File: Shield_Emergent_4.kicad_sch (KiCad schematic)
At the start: 32 parts, among them J1 TF31-18S-0.5SH_800_, J2 Conn_01x04_Socket, J3 TF31-18S-0.5SH_800_, J5 Conn_01x02_Socket, J6 Conn_01x02_Socket, U3 SP3012-06UTG, U4 SP3012-06UTG, X1 USB_C_24pins

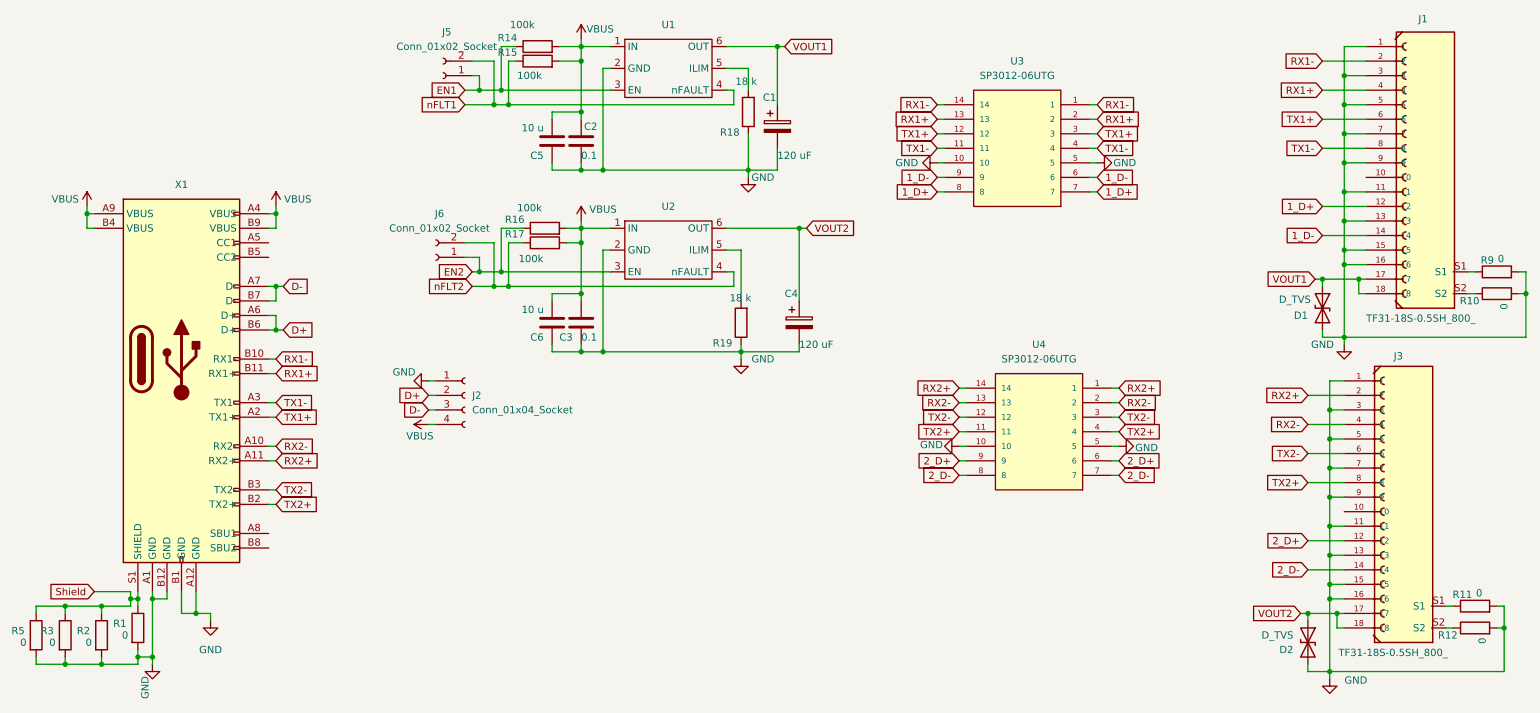
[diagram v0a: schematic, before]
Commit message: v0.2 draft routing
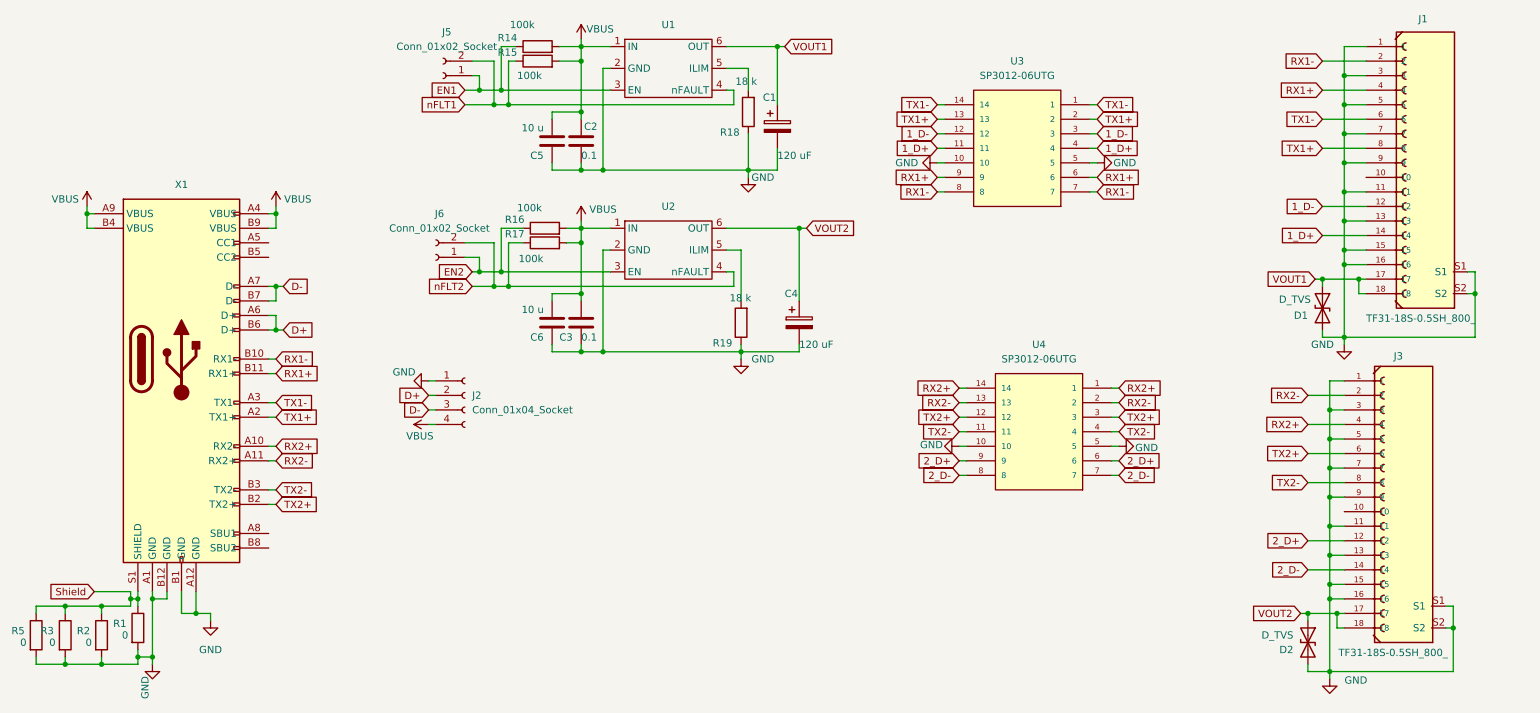
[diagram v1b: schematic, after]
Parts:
- removed R10, R11, R12, R9: 0, Resistor_SMD:R_0201_0603Metric_Pad0.64x0.40mm_HandSolder, symbol Device:R
- C2, C3, C5, C6: footprint Capacitor_SMD:C_0603_1608Metric_Pad1.08x0.95mm_HandSolder -> Capacitor_SMD:C_0402_1005Metric
- R14, R15, R16, R17, R18, R19: footprint Resistor_SMD:R_0603_1608Metric_Pad0.98x0.95mm_HandSolder -> Resistor_SMD:R_0402_1005Metric
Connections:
- net 1_D+: now also J1.14, U3.11, U3.4; no longer J1.12, U3.7, U3.8
- net 1_D-: now also J1.12, U3.12, U3.3; no longer J1.14, U3.6, U3.9
- net GND: now also J1.S1, J1.S2, J3.S1, J3.S2
- net RX1+: now also U3.6, U3.9; no longer U3.13, U3.2
- net RX1-: now also U3.7, U3.8; no longer U3.1, U3.14
- net RX2+: now also J3.4, X1.A10 (RX2-); no longer J3.2, X1.A11 (RX2+)
- net RX2-: now also J3.2, X1.A11 (RX2+); no longer J3.4, X1.A10 (RX2-)
- net TX1+: now also J1.8, U3.13, U3.2; no longer J1.6, U3.12, U3.3
- net TX1-: now also J1.6, U3.1, U3.14; no longer J1.8, U3.11, U3.4
- net TX2+: now also J3.6, U4.12, U4.3; no longer J3.8, U4.11, U4.4
- net TX2-: now also J3.8, U4.11, U4.4; no longer J3.6, U4.12, U4.3

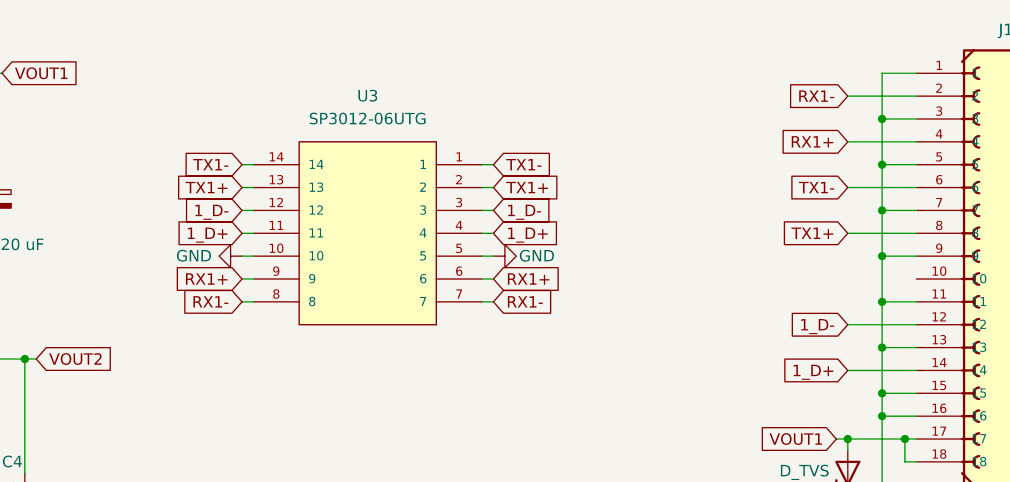
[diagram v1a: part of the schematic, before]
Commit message: v0.3 conceptual routing was added
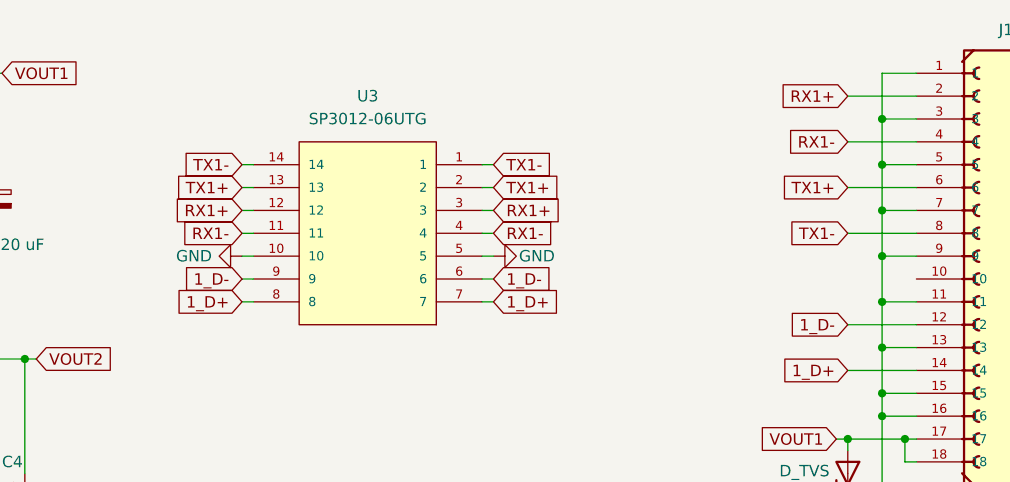
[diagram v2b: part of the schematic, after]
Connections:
- net 1_D+: now also U3.7, U3.8; no longer U3.11, U3.4
- net 1_D-: now also U3.6, U3.9; no longer U3.12, U3.3
- net RX1+: now also J1.2, U3.12, U3.3; no longer J1.4, U3.6, U3.9
- net RX1-: now also J1.4, U3.11, U3.4; no longer J1.2, U3.7, U3.8
- net TX1+: now also J1.6; no longer J1.8
- net TX1-: now also J1.8; no longer J1.6
